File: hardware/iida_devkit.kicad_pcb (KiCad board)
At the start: 4 copper layers, 123.6 x 55.6 mm, 142 parts, among them J1 USB4085-GF-A, J10 PRPC004SAAN-RC, J11 PRPC001DAAN-RC, J12 PRPC006SAAN-RC, J13 SIM8070-6-0-11-00-A, J2 B2B-PH-K-S, J3 PRPC001DAAN-RC, J4 PRPC001DAAN-RC, J5 PRPC001DAAN-RC, J6 TC2050, J7 PRPC006SAAN-RC, J8 PRPC001DAAN-RC, J9 PRPC006SAAN-RC, Q1 FDN338P, Q2 FDN338P, Q3 FDN338P, Q4 MMBT3904, U1 USBLC6-2SC6, U2 TLV76733DGNR, U3 AT25SF081B-SSHD-B, U4 MCP9808, U5 STM32L552CEU6, U6 SN74AVC4T245PW, U7 SARA-R500S-61B, Y1 ECS-160-9-37-CKM-TR3, Y2 ABS05-32.768KHZ-9-T

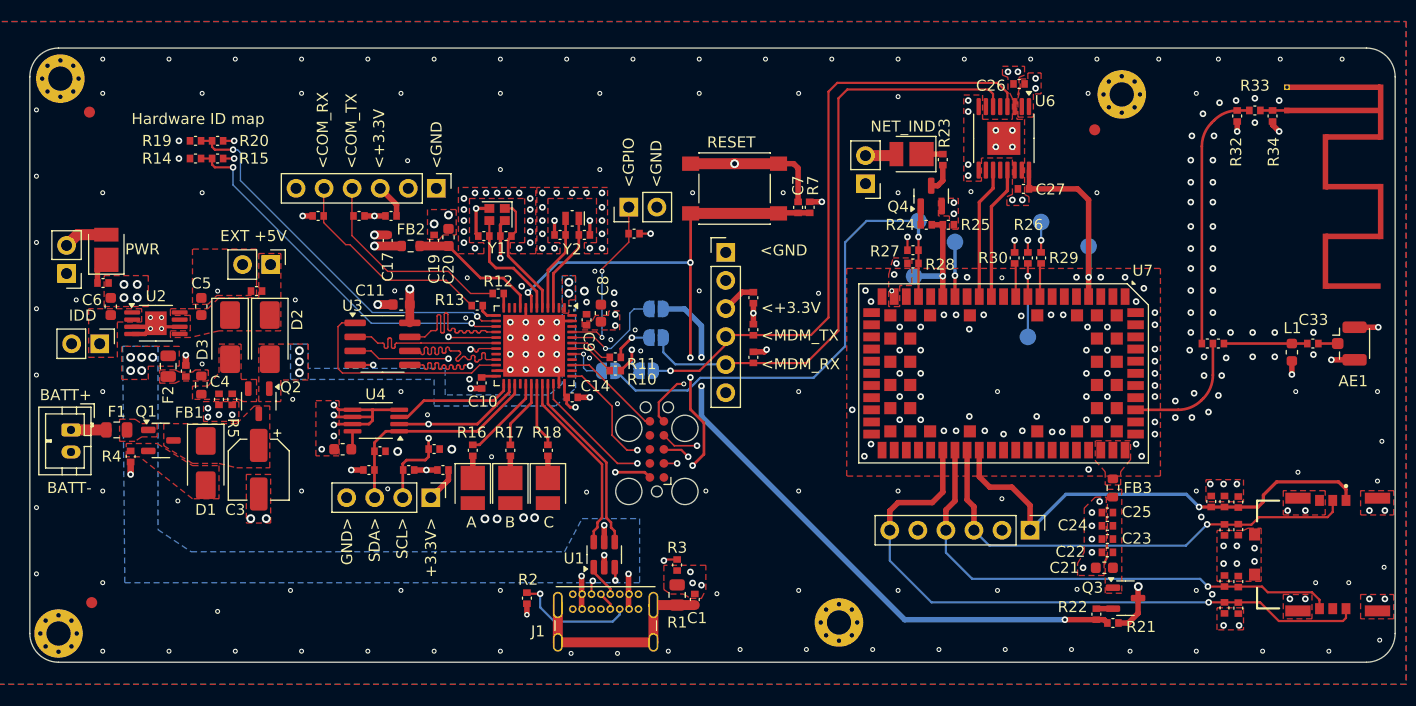
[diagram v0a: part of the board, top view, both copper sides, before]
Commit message: HW: Improve thermals, silkscreen and schematic
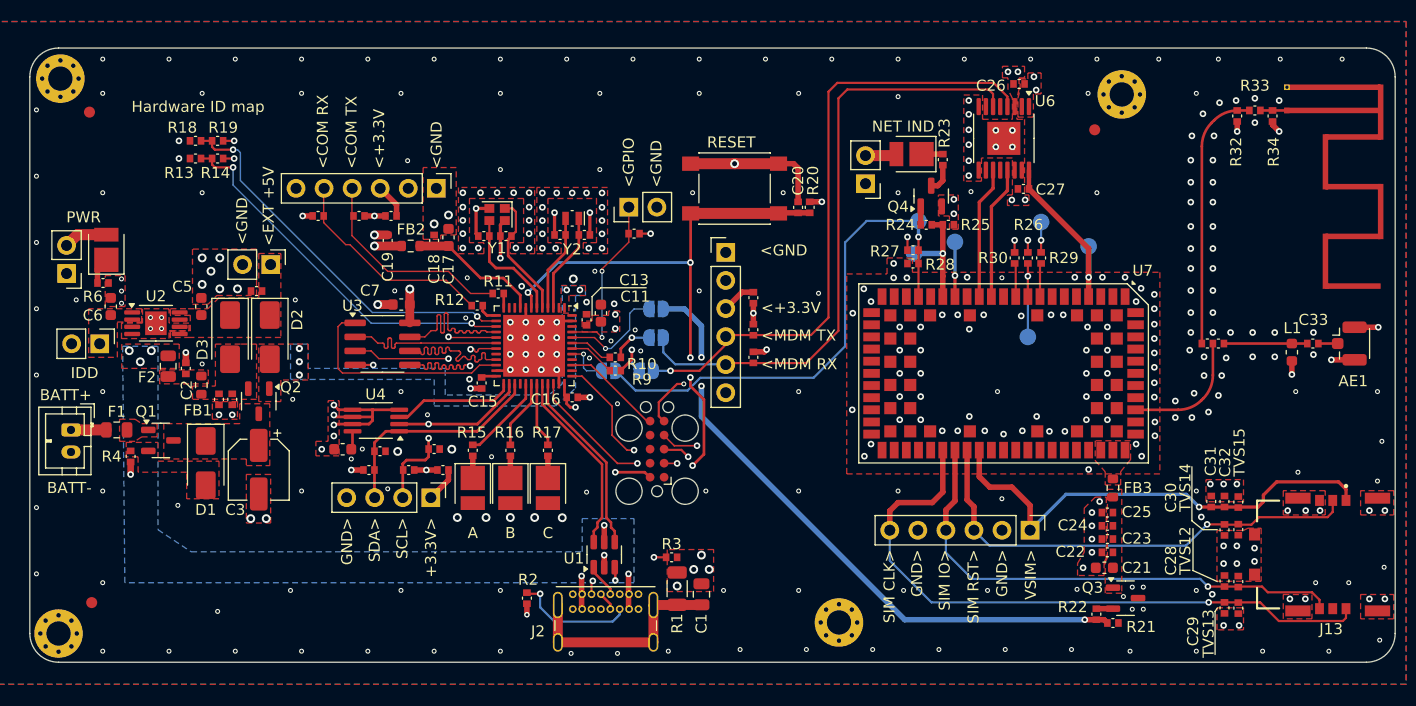
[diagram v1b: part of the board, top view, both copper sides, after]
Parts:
- removed the J6 at (140.2, 108.7)
- added J1: Tag-Connect 2050, Connector:Tag-Connect_TC2050-IDC-FP_2x05_P1.27mm_Vertical, F.Cu at (140.2, 108.7)
- C1: footprint perfect_footprints:0402_1005_perfect -> Capacitor_SMD:C_0805_2012Metric
- R1: footprint Resistor_SMD:R_0805_2012Metric -> Resistor_SMD:R_1206_3216Metric
- moved TP1 2.05 mm to (163.4, 91.0)
- moved R3 0.86 mm to (141.5, 118.5), turned to 180 degrees
- moved C1 0.77 mm to (144.2, 121.8)
- moved R1 0.57 mm to (142.0, 121.3)
- moved C2 0.24 mm to (97.5, 101.4)
- renumbered C15 to C10, C8 to C11, C16 to C12, C9 to C13, C18 to C14, C10 to C15, C14 to C16, C20 to C17, C19 to C18, C17 to C19, C7 to C20, C11 to C7, C12 to C8, C13 to C9, J1 to J2, J2 to J3, J3 to J4, J4 to J5, J5 to J6, R11 to R10, R12 to R11, R13 to R12, R14 to R13, R15 to R14, R16 to R15, R17 to R16, R18 to R17, R19 to R18, R20 to R19, R7 to R20, R8 to R7, R9 to R8, R10 to R9
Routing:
- net GND: track 89.3 -> 84.6 mm, vias 377 -> 382
- net /MCU/+3.3V: track 27.3 -> 22.7 mm, vias 19 -> 26
- net /Modem/V_INT: track 19.1 -> 16.5 mm
- net Net-(J2-CC1): track 9.69 -> 8.77 mm
- net Net-(J2-SHIELD): track 19.2 -> 19.8 mm
- net Net-(U1-VBUS): vias 8 -> 6
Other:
- board text added: "<COM RX"
- board text added: "<COM TX"
- board text added: "<EXT +5V"
- board text added: "<MDM RX"
- board text added: "<MDM TX"
- board text added: "NET IND"
- board text added: "SIM CLK>"
- board text added: "SIM IO>"
- board text added: "SIM RST>"
- board text added: "VSIM>"
- board text removed: "<COM_RX"
- board text removed: "<COM_TX"
- board text removed: "<MDM_RX"
- board text removed: "<MDM_TX"
- board text removed: "EXT +5V"
- board text removed: "NET_IND"

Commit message: HW: Update components
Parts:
- J2: value USB4085-GF-A -> USB4110-GF-A; footprint Connector_USB:USB_C_Receptacle_GCT_USB4085 -> Connector_USB:USB_C_Receptacle_GCT_USB4110
- LED1, LED2, LED3, LED4, LED5: value LS T67K-K1L2-1-0-2-R18-Z -> 150141YS73100
- Q1, Q2, Q3: value FDN338P -> IRLML2246TRPBF
- moved R2 15.2 mm to (142.9, 117.5), turned to 180 degrees
- moved R3 13.7 mm to (128.1, 121.5), turned to -90 degrees
- moved J2 4.42 mm to (135.4, 125.2)
- moved C1 1.72 mm to (145.6, 120.8)
- moved R1 1.72 mm to (143.4, 120.3)
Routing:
- net Net-(J2-SHIELD): track 19.8 -> 0.00 mm
- net Net-(U1-VBUS): track 7.67 -> 4.53 mm
- net GND: track 84.6 -> 87.5 mm, vias 382 -> 386
- net Net-(J2-CC2): track 10.8 -> 8.03 mm, vias 1 -> 0
- net /Power/USB_DP_IN: track 4.91 -> 4.60 mm, vias 1 -> 0
- added copper zone on F.Cu, net Net-(J2-SHIELD)

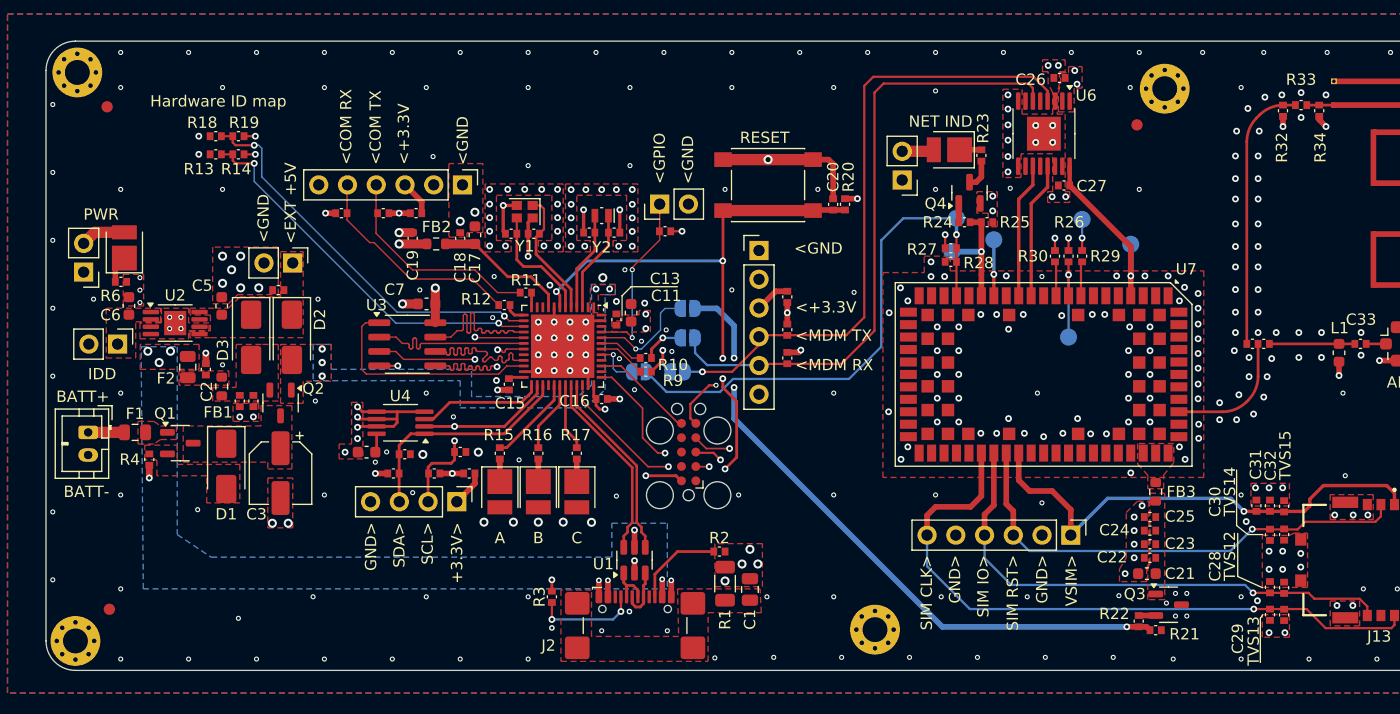
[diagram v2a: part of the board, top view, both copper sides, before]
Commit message: HW: Update VBAT, schema and layout
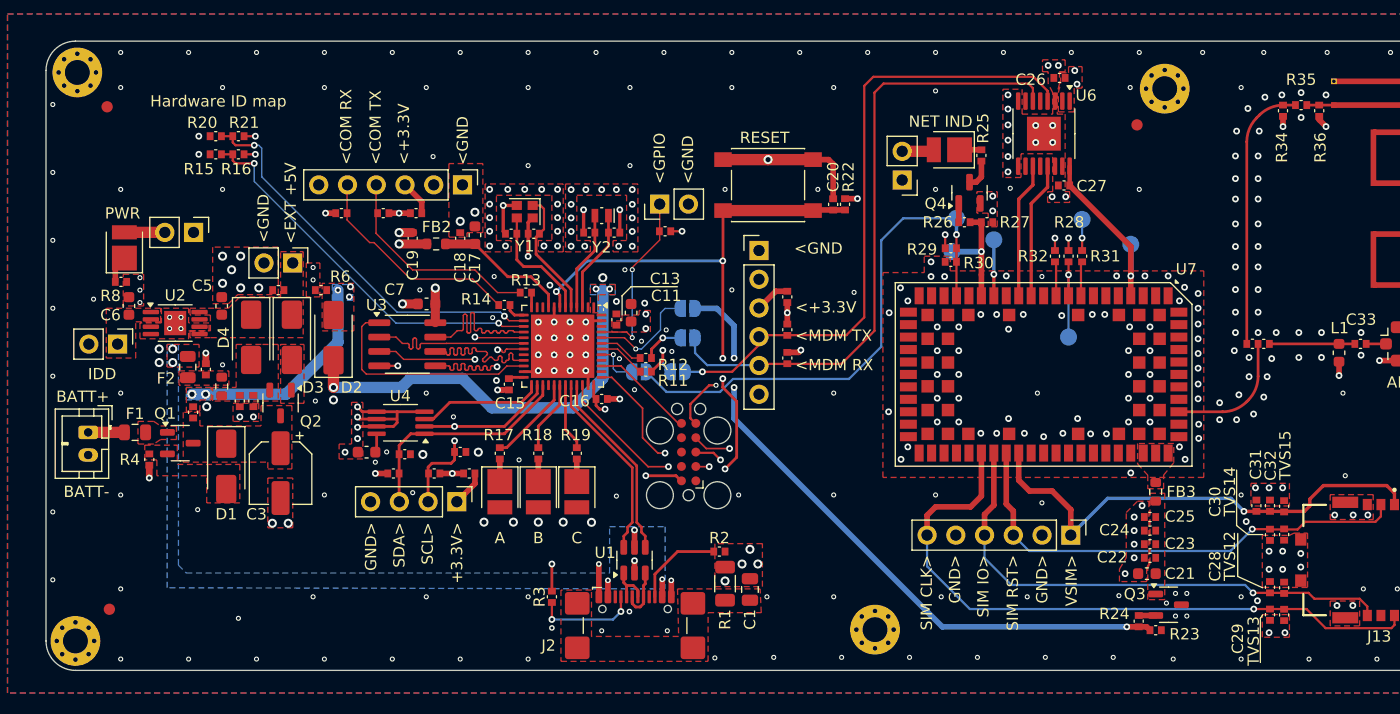
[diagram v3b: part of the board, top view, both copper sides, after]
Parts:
- added D2: CDBA140LL-HF, Diode_SMD:D_SMA, F.Cu at (108.8, 98.6)
- added R5: 2.2 kΩ, perfect_footprints:0402_1005_perfect, F.Cu at (96.4, 105.2)
- added R6: 10 kΩ, perfect_footprints:0402_1005_perfect, F.Cu at (107.7, 94.4)
- moved J6 10.3 mm to (96.4, 89.3), turned to -90 degrees
- renumbered D2 to D3, D3 to D4, R8 to R10, R9 to R11, R10 to R12, R11 to R13, R12 to R14, R13 to R15, R14 to R16, R15 to R17, R16 to R18, R17 to R19, R18 to R20, R19 to R21, R20 to R22, R21 to R23, R22 to R24, R23 to R25, R24 to R26, R25 to R27, R26 to R28, R27 to R29, R28 to R30, R29 to R31, R30 to R32, R31 to R33, R32 to R34, R33 to R35, R34 to R36, R5 to R7, R6 to R8, R7 to R9
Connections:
- D3 pad 2: /MCU/+BATT -> Net-(D3-A)
- Q2 pad 1: /MCU/+BATT -> Net-(D3-A)
- U5 pad 1: /MCU/+BATT -> /MCU/VBAT
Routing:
- net /MCU/VBAT: track 0.00 -> 36.5 mm, vias 0 -> 3
- net Net-(D2-A): track 0.00 -> 19.4 mm, vias 0 -> 4
- net GND: track 87.5 -> 90.3 mm, vias 386 -> 392
- net Net-(U1-VBUS): vias 6 -> 5
- net /MCU/+BATT: vias 5 -> 0
- added copper zone on B.Cu, net /MCU/VBAT
- added copper zone on F.Cu, net /MCU/VBAT
- added copper zone on B.Cu, net Net-(D2-A)
- added copper zone on F.Cu, net Net-(D2-A)
- added copper zone on F.Cu, net Net-(D3-A)
- removed copper zone on B.Cu, net /MCU/+BATT
- removed copper zone on F.Cu, net /MCU/+BATT

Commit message: HW: Start layout all over again
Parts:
- removed AE1: U.FL-R-SMT-1(10), Connector_Coaxial:U.FL_Hirose_U.FL-R-SMT-1_Vertical
- removed AE2: PCB antenna, PCB_antenna:800MHz_antenna
- removed C1: 4.7 nF, Capacitor_SMD:C_0805_2012Metric
- removed C10, C12, C14, C8: 8 pF, perfect_footprints:0402_1005_perfect
- removed C11, C17, C5, C6, C7, C9: 4.7 µF, Capacitor_SMD:C_0603_1608Metric
- removed C13, C15, C16, C18, C19, C2, C20, C22, C26, C27, C32, C4: 100 nF, perfect_footprints:0402_1005_perfect
- removed C21: 10 µF, Capacitor_SMD:C_0603_1608Metric
- removed C23: 10 nF, perfect_footprints:0402_1005_perfect
- removed C24: 68 pF, perfect_footprints:0402_1005_perfect
- removed C25: 15 pF, perfect_footprints:0402_1005_perfect
- removed C28, C29, C30, C31, C33: 33 pF, perfect_footprints:0402_1005_perfect
- removed C3: 100 µF, Capacitor_SMD:CP_Elec_5x5.3
- removed D1, D2, D3, D4: CDBA140LL-HF, Diode_SMD:D_SMA
- removed F1, F2: 2A, Fuse:Fuse_0805_2012Metric
- removed FB1, FB2: 120 Ω @ 100 MHz, Resistor_SMD:R_0603_1608Metric
- removed FB3: 260 Ω @ 1 GHz, Resistor_SMD:R_0603_1608Metric
- removed FID1, FID2, FID3: Fiducial, Fiducial:Fiducial_1mm_Mask2mm
- removed H1, H2, H3, H4: MountingHole_Pad, MountingHole:MountingHole_2.2mm_M2_Pad_Via
- removed J1: Tag-Connect 2050, Connector:Tag-Connect_TC2050-IDC-FP_2x05_P1.27mm_Vertical
- removed J10: PRPC004SAAN-RC, Connector_PinHeader_2.54mm:PinHeader_1x04_P2.54mm_Vertical
- removed J11, J4, J5, J6, J8: PRPC001DAAN-RC, Connector_PinHeader_2.54mm:PinHeader_1x02_P2.54mm_Vertical
- removed J12, J7, J9: PRPC006SAAN-RC, Connector_PinHeader_2.54mm:PinHeader_1x06_P2.54mm_Vertical
- removed J13: SIM8070-6-0-11-00-A, SIM8070-6-0-11-00-A:SIM8070-6-0-11-00-A
- removed J2: USB4110-GF-A, Connector_USB:USB_C_Receptacle_GCT_USB4110
- removed J3: B2B-PH-K-S, Connector_JST:JST_PH_B2B-PH-K_1x02_P2.00mm_Vertical
- removed JP1, JP2, JP3, JP4: SolderJumper_2_Open, Jumper:SolderJumper-2_P1.3mm_Open_RoundedPad1.0x1.5mm
- removed L1: 39 nH, Inductor_SMD:L_0603_1608Metric
- removed LED1, LED2, LED3, LED4, LED5: 150141YS73100, LED_SMD:LED_PLCC_2835
- removed Q1, Q2, Q3: IRLML2246TRPBF, Package_TO_SOT_SMD:SOT-23-3
- removed Q4: MMBT3904, Package_TO_SOT_SMD:SOT-23
- removed R1: 1 MΩ, Resistor_SMD:R_1206_3216Metric
- removed R10, R17, R18, R19, R24, R25, R5, R8, R9: 2.2 kΩ, perfect_footprints:0402_1005_perfect
- removed R11, R12, R13, R14: 22 Ω, perfect_footprints:0402_1005_perfect
- removed R15, R16, R20, R21, R28, R31, R32, R34, R35, R36: 0 Ω, perfect_footprints:0402_1005_perfect
- removed R2, R3: 5.1 kΩ, perfect_footprints:0402_1005_perfect
- removed R22, R23, R26, R27, R29, R30, R4, R6, R7: 10 kΩ, perfect_footprints:0402_1005_perfect
- removed R33: 0 Ω, perfect_footprints:0hm_choice
- removed SW_SPST1: PTS645SK50SMTR92 LFS, Button_Switch_SMD:SW_SPST_PTS645
- removed TP1, TP2, TP3, TP4, TP5, TP6: TestPoint, TestPoint:TestPoint_Pad_D1.5mm
- removed TVS1, TVS10, TVS11, TVS12, TVS13, TVS14, TVS15, TVS2, TVS3, TVS4, TVS5, TVS6, TVS7, TVS8, TVS9: PE1605M1Q_R1_00001, perfect_footprints:0402_1005_perfect
- removed U1: USBLC6-2SC6, Package_TO_SOT_SMD:SOT-23-6
- removed U2: TLV76733DGNR, Package_SO:MSOP-8-1EP_3x3mm_P0.65mm_EP1.95x2.15mm
- removed U3: AT25SF081B-SSHD-B, Package_SO:SOIC-8_3.9x4.9mm_P1.27mm
- removed U4: MCP9808, Package_SO:MSOP-8_3x3mm_P0.65mm
- removed U5: STM32L552CEU6, Package_DFN_QFN:QFN-48-1EP_7x7mm_P0.5mm_EP5.6x5.6mm
- removed U6: SN74AVC4T245PW, Package_SO:TSSOP-16-1EP_4.4x5mm_P0.65mm_EP3x3mm
- removed U7: SARA-R500S-61B, RF_GSM:ublox_SARA_LGA-96
- removed Y1: ECS-160-9-37-CKM-TR3, Crystal:Crystal_SMD_2016-4Pin_2.0x1.6mm
- removed Y2: ABS05-32.768KHZ-9-T, Crystal:Crystal_SMD_MicroCrystal_CM9V-T1A-2Pin_1.6x1.0mm
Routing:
- net GND: track 90.3 -> 0.00 mm, vias 392 -> 0
- net /MCU/NRST: track 62.5 -> 0.00 mm, vias 6 -> 0
- net /Modem/SIM_CLK: track 58.3 -> 0.00 mm, vias 1 -> 0
- net /MCU/~{MODEM_PWR_EN}: track 56.8 -> 0.00 mm, vias 3 -> 0
- net /MCU/MODEM_TX: track 55.9 -> 0.00 mm, vias 1 -> 0
- net /MCU/MODEM_RX: track 55.5 -> 0.00 mm
- net /MCU/~{MODEM_RESET}: track 46.9 -> 0.00 mm, vias 1 -> 0
- net /Modem/SIM_IO: track 46.0 -> 0.00 mm, vias 1 -> 0
- net /Modem/VSIM: track 43.3 -> 0.00 mm, vias 1 -> 0
- net /Modem/SIM_RST: track 42.9 -> 0.00 mm, vias 1 -> 0
- net /MCU/VBAT: track 36.5 -> 0.00 mm, vias 3 -> 0
- net Net-(U5-PA4): track 35.3 -> 0.00 mm, vias 2 -> 0
- net Net-(U5-PA5): track 34.3 -> 0.00 mm, vias 2 -> 0
- net /Antenna/ANT_PCB_SEL: track 23.9 -> 0.00 mm
- net /MCU/+3.3V: track 22.7 -> 0.00 mm, vias 26 -> 0
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- removed copper zone on B.Cu, net /MCU/+3.3V
- removed copper zone on F.Cu, net /MCU/+3.3V
- removed copper zone on B.Cu, net /MCU/VBAT
- removed copper zone on F.Cu, net /MCU/VBAT
- removed copper zone on F.Cu, net /Modem/+3.3V_MDM
- removed copper zone on F.Cu, net /Modem/+3.3V_MDM_UNFILTERED
- removed copper zone on F.Cu, net GND
- removed copper zone on In1.Cu, net GND
- removed copper zone on In2.Cu, net GND
- removed copper zone on F.Cu, net Net-(C2-Pad1)
- removed copper zone on F.Cu, net Net-(D1-A)
- removed copper zone on F.Cu, net Net-(D1-K)
- removed copper zone on B.Cu, net Net-(D2-A)
- removed copper zone on F.Cu, net Net-(D2-A)
- removed copper zone on F.Cu, net Net-(D3-A)
- removed copper zone on F.Cu, net Net-(D3-K)
- removed copper zone on F.Cu, net Net-(D4-A)
- removed copper zone on F.Cu, net Net-(J2-SHIELD)
- removed copper zone on F.Cu, net Net-(J5-Pin_1)
- removed copper zone on F.Cu, net Net-(Q1-D)
- removed copper zone on B.Cu, net Net-(U1-VBUS)
- removed copper zone on F.Cu, net Net-(U1-VBUS)
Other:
- board outline removed
- board text removed: "+3.3V>"
- board text removed: "<+3.3V"
- board text removed: "<COM RX"
- board text removed: "<COM TX"
- board text removed: "<EXT +5V"
- board text removed: "<GND"
- board text removed: "<GPIO"
- board text removed: "<MDM RX"
- board text removed: "<MDM TX"
- board text removed: "A"
- board text removed: "B"
- board text removed: "BATT+"
- board text removed: "BATT-"
- board text removed: "C"
- board text removed: "GND>"
- board text removed: "Hardware ID map"
- board text removed: "IDD"
- board text removed: "Iida devkit v4.2.0"
- board text removed: "NET IND"
- board text removed: "PWR"
- board text removed: "RESET"
- board text removed: "SCL>"
- board text removed: "SDA>"
- board text removed: "SIM CLK>"
- board text removed: "SIM IO>"
- board text removed: "SIM RST>"
- board text removed: "VSIM>"
